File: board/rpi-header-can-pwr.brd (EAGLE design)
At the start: 87 x 56.5 mm, 62 parts, among them IC1 MCP2515-E/SO, J1 U.FL, U3 BME280, U4 RFM69HCW, U5 INA219BIDCNT, X1 RJ45-8L21-S, X2 RASPI_BOARD_B+#_E3

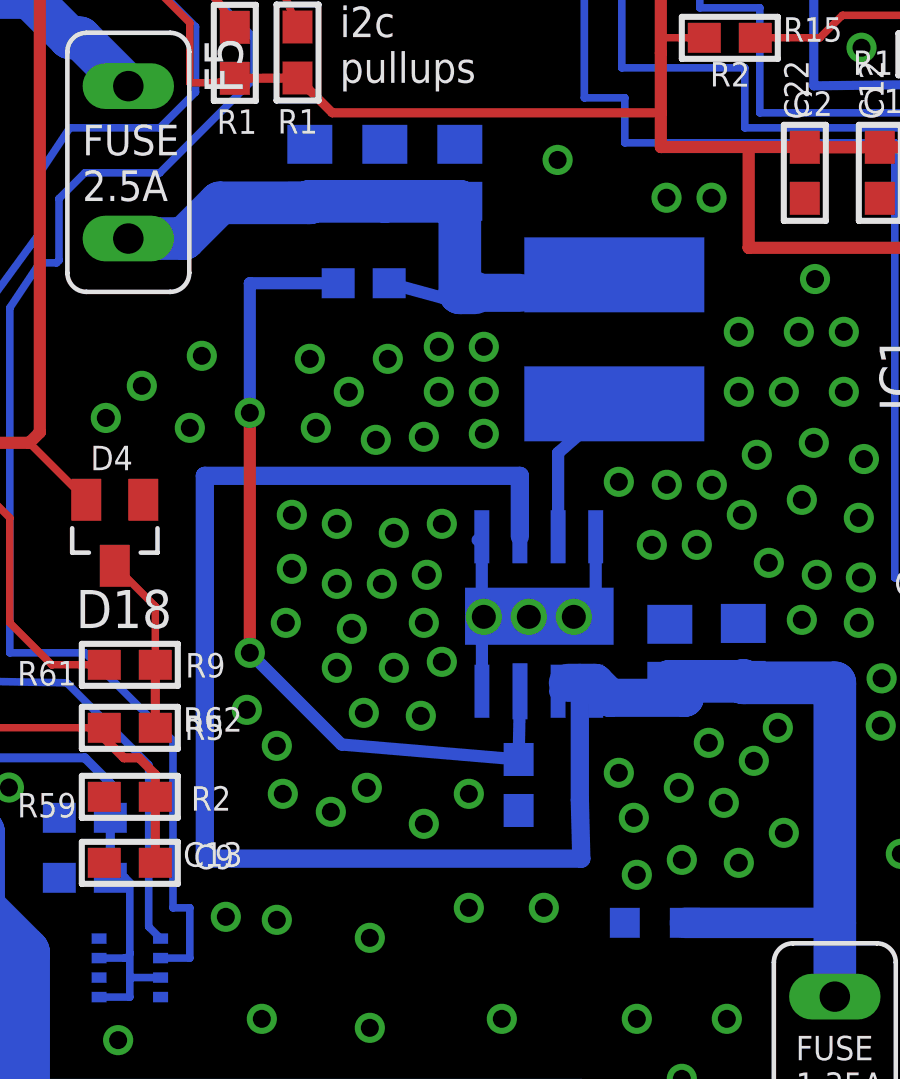
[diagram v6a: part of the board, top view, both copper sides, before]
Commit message: increase ST1S10 pad size
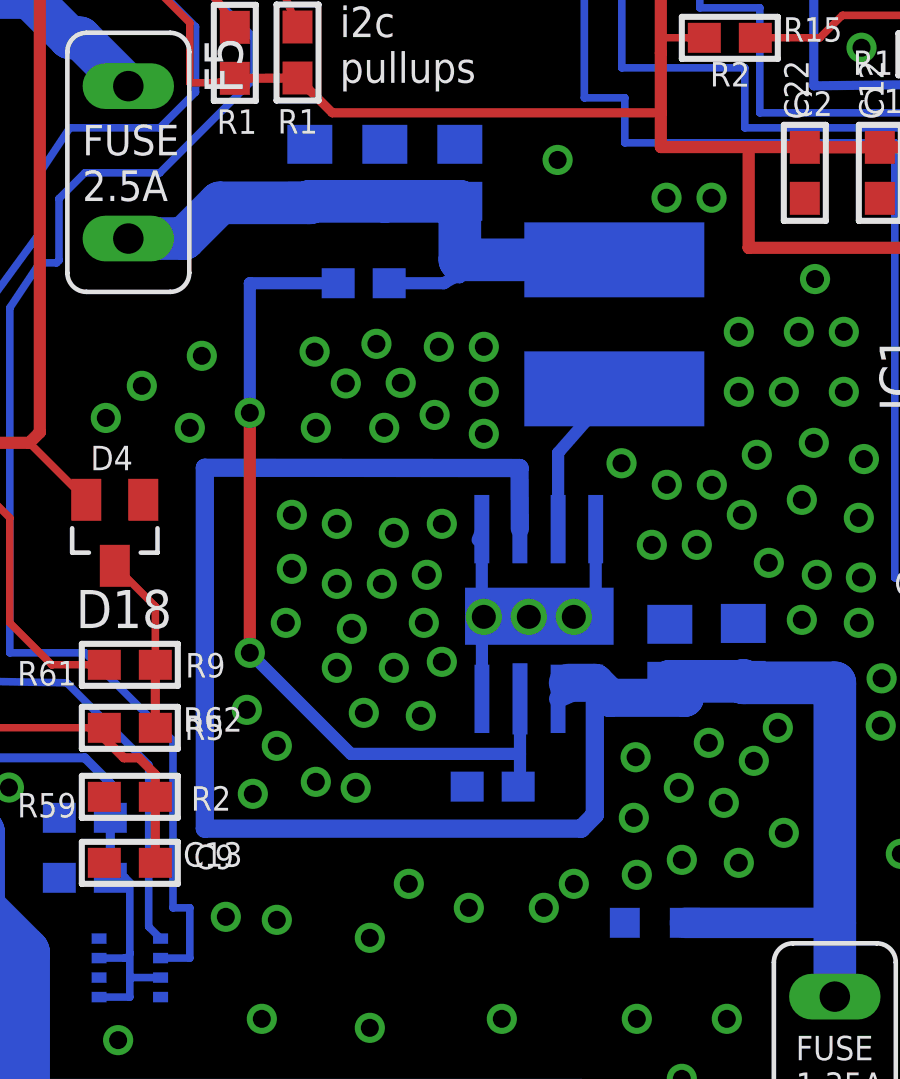
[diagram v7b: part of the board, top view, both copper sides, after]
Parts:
- moved R2 0.87 mm to (45.1, 22.0), turned to 180 degrees
- moved U$2 0.50 mm to (49.1, 37.5)
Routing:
- net N$8: track 23.2 -> 21.7 mm
- net GND: track 25.4 -> 26.4 mm
- net N$1: track 27.8 -> 28.7 mm
- net +12V: track 73.9 -> 73.2 mm
